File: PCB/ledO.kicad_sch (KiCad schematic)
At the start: 14 parts, among them Q31 Q_PNP_BCE, Q32 Q_NPN_BCE

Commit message: made some Changes
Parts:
- removed Q31: Q_PNP_BCE, Package_TO_SOT_SMD:SOT-23, symbol Device:Q_PNP_BCE
- removed R31: 12k, Resistor_SMD:R_1206_3216Metric_Pad1.30x1.75mm_HandSolder, symbol Device:R
- removed R34: 1k, Resistor_SMD:R_1206_3216Metric_Pad1.30x1.75mm_HandSolder, symbol Device:R
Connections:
- net VCC: now also D31.2 (A), D32.2 (A), D33.2 (A), D34.2 (A), D35.2 (A), D36.2 (A), D37.2 (A), D38.2 (A)
- net LEDA: now reaches Q32.1 (B)
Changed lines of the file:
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@@
   (junction (at 145.415 70.485) (diameter 0) (color 0 0 0 0)
   )
+  (junction (at 140.97 70.485) (diameter 0) (color 0 0 0 0)
+  )
   (junction (at 153.035 79.375) (diameter 0) (color 0 0 0 0)
   )
@@
   (junction (at 125.095 79.375) (diameter 0) (color 0 0 0 0)
   )
-  (junction (at 140.97 70.485) (diameter 0) (color 0 0 0 0)
-  )
   (junction (at 121.285 79.375) (diameter 0) (color 0 0 0 0)
   )
@@
     (stroke (width 0) (type default) (color 0 0 0 0))
   )
+  (wire (pts (xy 136.525 70.485) (xy 140.97 70.485))
+    (stroke (width 0) (type default) (color 0 0 0 0))
+  )
   (wire (pts (xy 140.97 70.485) (xy 145.415 70.485))
     (stroke (width 0) (type default) (color 0 0 0 0))
   )
-  (wire (pts (xy 136.525 70.485) (xy 140.97 70.485))
-    (stroke (width 0) (type default) (color 0 0 0 0))
-  )
   (wire (pts (xy 153.035 78.105) (xy 153.035 79.375))
     (stroke (width 0) (type default) (color 0 0 0 0))
@@
     (stroke (width 0) (type default) (color 0 0 0 0))
   )
-  (hierarchical_label "LEDA_D" (shape input) (at 126.365 97.155 180)
+  (hierarchical_label "LEDA" (shape input) (at 133.985 97.155 180)
     (effects (font (size 1.27 1.27)) (justify right))
-  )
-  (hierarchical_label "LEDA_EN" (shape input) (at 125.73 65.405 180)
-    (effects (font (size 1.27 1.27)) (justify right))
-  )
-  (symbol (lib_id "Device:R") (at 130.175 97.155 90) (unit 1)
-    (in_bom yes) (on_board yes) (fields_autoplaced)
-    (property "Reference" "R34" (id 0) (at 130.175 90.805 90))
-    (property "Value" "1k" (id 1) (at 130.175 93.345 90))
-    (property "Footprint" "Resistor_SMD:R_1206_3216Metric_Pad1.30x1.75mm_HandSolder" (id 2) (at 130.175 98.933 90)
-      (effects (font (size 1.27 1.27)) hide)
-    )
-    (property "Datasheet" "~" (id 3) (at 130.175 97.155 0)
-      (effects (font (size 1.27 1.27)) hide)
-    )
-    (property "Price" "0.0021" (id 4) (at 130.175 97.155 0)
-      (effects (font (size 1.27 1.27)) hide)
-    )
-    (pin "1")
-    (pin "2")
   )
   (symbol (lib_id "Device:LED") (at 145.415 74.295 90) (unit 1)
@@
     (pin "2")
   )
-  (symbol (lib_id "power:VCC") (at 140.97 60.325 0) (unit 1)
+  (symbol (lib_id "power:VCC") (at 140.97 70.485 0) (unit 1)
     (in_bom yes) (on_board yes) (fields_autoplaced)
-    (property "Reference" "#PWR031" (id 0) (at 140.97 64.135 0)
-      (effects (font (size 1.27 1.27)) hide)
-    )
-    (property "Value" "VCC" (id 1) (at 140.97 54.61 0))
-    (property "Footprint" "" (id 2) (at 140.97 60.325 0)
-      (effects (font (size 1.27 1.27)) hide)
-    )
-    (property "Datasheet" "" (id 3) (at 140.97 60.325 0)
-      (effects (font (size 1.27 1.27)) hide)
-    )
-    (pin "1")
-  )
-  (symbol (lib_id "Device:Q_PNP_BCE") (at 138.43 65.405 0) (mirror x) (unit 1)
-    (in_bom yes) (on_board yes) (fields_autoplaced)
-    (property "Reference" "Q31" (id 0) (at 143.51 64.1349 0)
-      (effects (font (size 1.27 1.27)) (justify left))
-    )
-    (property "Value" "Q_PNP_BCE" (id 1) (at 143.51 66.6749 0)
-      (effects (font (size 1.27 1.27)) (justify left))
-    )
-    (property "Footprint" "Package_TO_SOT_SMD:SOT-23" (id 2) (at 143.51 67.945 0)
-      (effects (font (size 1.27 1.27)) hide)
-    )
-    (property "Datasheet" "https://www.lcsc.com/product-detail/Bipolar-Transistors-BJT_Guangdong-Hottech-S8550_C181159.html" (id 3) (at 138.43 65.405 0)
-      (effects (font (size 1.27 1.27)) hide)
-    )
-    (pin "1")
-    (pin "2")
-    (pin "3")
+    (property "Reference" "#PWR031" (id 0) (at 140.97 74.295 0)
+      (effects (font (size 1.27 1.27)) hide)
+    )
+    (property "Value" "VCC" (id 1) (at 140.97 64.77 0))
+    (property "Footprint" "" (id 2) (at 140.97 70.485 0)
+      (effects (font (size 1.27 1.27)) hide)
+    )
+    (property "Datasheet" "" (id 3) (at 140.97 70.485 0)
+      (effects (font (size 1.27 1.27)) hide)
+    )
+    (pin "1")
   )
   (symbol (lib_id "Device:LED") (at 153.035 74.295 90) (unit 1)
@@
       (effects (font (size 1.27 1.27)) hide)
     )
-    (pin "1")
-    (pin "2")
-  )
-  (symbol (lib_id "Device:R") (at 129.54 65.405 90) (unit 1)
-    (in_bom yes) (on_board yes) (fields_autoplaced)
-    (property "Reference" "R31" (id 0) (at 129.54 59.69 90))
-    (property "Value" "12k" (id 1) (at 129.54 62.23 90))
-    (property "Footprint" "Resistor_SMD:R_1206_3216Metric_Pad1.30x1.75mm_HandSolder" (id 2) (at 129.54 67.183 90)
-      (effects (font (size 1.27 1.27)) hide)
-    )
-    (property "Datasheet" "~" (id 3) (at 129.54 65.405 0)
-      (effects (font (size 1.27 1.27)) hide)
-    )

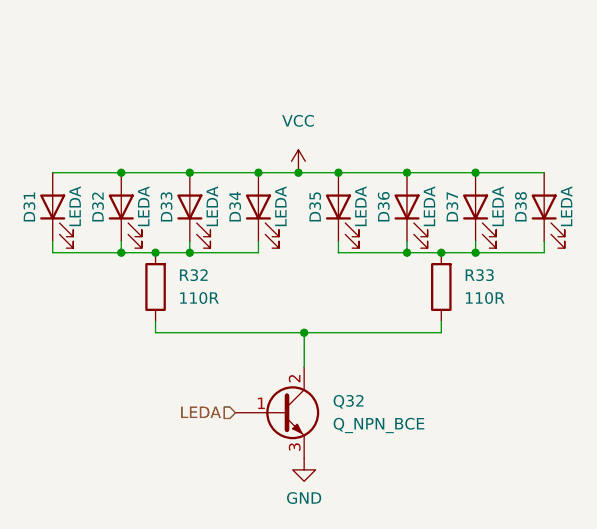
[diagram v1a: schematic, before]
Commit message: added Capacitor and updated PCB
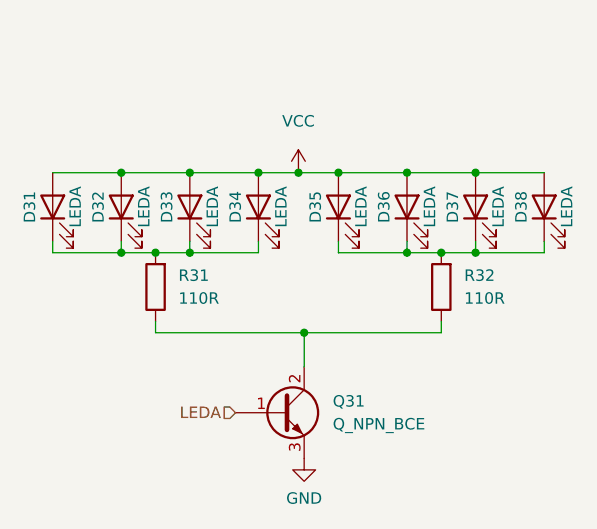
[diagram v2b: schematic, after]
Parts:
- renumbered Q32 to Q31, R32 to R31, R33 to R32
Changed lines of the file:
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@@
   (symbol (lib_id "Device:R") (at 156.845 83.185 180) (unit 1)
     (in_bom yes) (on_board yes) (fields_autoplaced)
-    (property "Reference" "R33" (id 0) (at 159.385 81.9149 0)
+    (property "Reference" "R32" (id 0) (at 159.385 81.9149 0)
       (effects (font (size 1.27 1.27)) (justify right))
     )
@@
   (symbol (lib_id "Device:Q_NPN_BCE") (at 139.065 97.155 0) (unit 1)
     (in_bom yes) (on_board yes) (fields_autoplaced)
-    (property "Reference" "Q32" (id 0) (at 144.78 95.8849 0)
+    (property "Reference" "Q31" (id 0) (at 144.78 95.8849 0)
       (effects (font (size 1.27 1.27)) (justify left))
     )
@@
   (symbol (lib_id "Device:R") (at 125.095 83.185 180) (unit 1)
     (in_bom yes) (on_board yes) (fields_autoplaced)
-    (property "Reference" "R32" (id 0) (at 127.635 81.9149 0)
+    (property "Reference" "R31" (id 0) (at 127.635 81.9149 0)
       (effects (font (size 1.27 1.27)) (justify right))
     )
